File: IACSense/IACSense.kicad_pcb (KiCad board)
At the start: 2 copper layers, 57 parts, among them P1 CONN_01X03, P2 CONN_01X03, P3 zcd, P4 event, U1 MCP39F521, U2 MCP970x, U3 MCP1754, U4 PIC16F18323_QFN, Y1 4MHz

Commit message: Update IACSense
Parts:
- added D1: MB8S, Yame_library:MBxS, F.Cu at (212.5, 85.0)
- added P5: Prog, Yame_library:HE10_14-5C-2.54-MR, F.Cu at (167.0, 47.0)
- added P6: nRF24L01+, Yame_library:HE10_14-2x4C-2.54-MR, F.Cu at (167.0, 108.0)
- added P7: I2C, Yame_library:HE10_14-3C-2.54-MR, F.Cu at (168.0, 100.0)
- FB1, FB2, R1, R2: moved to B.Cu
- U3: footprint TO_SOT_Packages_THT:TO-220_Neutral123_Vertical -> Yame_library:SOT23-MR
- moved Y1 92.3 mm to (207.5, 34.0)
- moved C3 83.7 mm to (231.0, 91.0)
- moved R8 83.2 mm to (230.5, 91.0)
- moved D2 82.2 mm to (210.0, 50.5)
- moved FB4 81.8 mm to (200.0, 41.5)
- moved R16 76.4 mm to (201.0, 49.5)
- moved R6 76.0 mm to (187.0, 39.5)
- moved R4 74.9 mm to (192.0, 44.0)
- moved R3 74.8 mm to (197.0, 48.0)
- moved R15 70.0 mm to (190.5, 49.0)
- moved C2 69.6 mm to (185.5, 46.0)
- moved R5 68.7 mm to (181.0, 44.5)
- moved R19 67.8 mm to (176.0, 43.0)
- moved F1 67.7 mm to (215.0, 92.5)
- moved P2 67.5 mm to (200.5, 62.0), turned to 180 degrees
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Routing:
- net /Line: track 0.00 -> 87.8 mm
- net /Ground: track 0.00 -> 74.7 mm
- net Net-(FB4-Pad1): track 0.00 -> 56.7 mm
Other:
- board outline added: 29 x 83 mm
- rule via_min_size: 0.4 -> 0.5

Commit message: update IACSense
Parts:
- C1, C11, C13, C2, C4, D1, FB3, FB4, R3, R4, R5, R6, R7, R8, R9, U1, U3: moved to B.Cu
- P1: value CONN_01X03 -> IN
- P2: value CONN_01X03 -> OUT
- P6: footprint Yame_library:HE10_14-2x4C-2.54-MR -> Yame_library:NRF24L01+
- moved C4 61.9 mm to (197.8, 83.5)
- moved R7 59.1 mm to (197.2, 86.2), turned to 270 degrees
- moved P6 58.2 mm to (221.4, 87.5), turned to 180 degrees
- moved R9 57.2 mm to (197.8, 82.0)
- moved U1 54.4 mm to (204.8, 74.1), turned to 180 degrees
- moved C13 54.3 mm to (197.6, 97.4)
- moved C11 50.6 mm to (197.7, 99.3)
- moved D2 49.4 mm to (201.6, 99.2)
- moved FB1 45.9 mm to (213.8, 116.0), turned to 90 degrees
- moved R4 45.6 mm to (197.2, 89.3), turned to 270 degrees
- moved U3 45.3 mm to (197.4, 94.3), turned to 270 degrees
- moved FB2 43.8 mm to (206.2, 118.6), turned to 270 degrees
- moved C3 40.6 mm to (198.6, 115.3)
- moved C1 40.2 mm to (200.2, 76.5), turned to 270 degrees
- moved R2 38.5 mm to (203.3, 118.3)
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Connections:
- FB2 pad 2: Net-(FB2-Pad2) -> /Neutral
- VR1 pad 2: Net-(FB2-Pad2) -> /Neutral
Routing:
- net /Neutral: track 0.00 -> 58.2 mm
- net Net-(FB4-Pad1): track 56.7 -> 32.7 mm

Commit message: Update IACSense
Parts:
- added C21: 10u, Yame_library:SM0805-MR, F.Cu at (208.9, 85.7)
- added FB5: BLM18AG102SN1D, Yame_library:SM0603-MR, F.Cu at (187.2, 81.8)
- C11, C13, C4, R4, R7, R9, U1, U3: moved to F.Cu
- R2: footprint Yame_library:SM0603-MR -> Yame_library:SM1206-MR
- R20: moved to B.Cu
- moved C17 89.8 mm to (225.3, 78.4), turned to 180 degrees
- moved D3 86.9 mm to (229.4, 75.3), turned to 90 degrees
- moved C6 83.8 mm to (219.7, 74.3), turned to 270 degrees
- moved C7 74.9 mm to (219.7, 79.9), turned to 90 degrees
- moved P5 71.3 mm to (224.7, 89.0), turned to 270 degrees
- moved C12 68.3 mm to (204.7, 72.0), turned to 270 degrees
- moved R17 67.9 mm to (229.4, 78.4), turned to 270 degrees
- moved R11 66.1 mm to (211.3, 73.9), turned to 270 degrees
- moved R13 65.3 mm to (221.2, 70.2), turned to 270 degrees
- moved C8 64.4 mm to (203.8, 84.2), turned to 270 degrees
- moved C15 64.1 mm to (213.6, 89.8), turned to 270 degrees
- moved C16 63.7 mm to (206.1, 84.8), turned to 270 degrees
- moved C5 63.4 mm to (201.0, 82.3), turned to 270 degrees
- moved P7 63.2 mm to (220.4, 64.7)
- moved C20 62.8 mm to (208.7, 73.0)
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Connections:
- P1 pad 1: /Ground -> /Neutral
- P1 pad 3: /Neutral -> /Ground
- P2 pad 1: Net-(FB4-Pad1) -> /Ground
- P2 pad 3: /Ground -> Net-(FB4-Pad1)
- R19 pad 2: /Vtemp -> Net-(R18-Pad2)
- R4 pad 2: Net-(F1-Pad1) -> Net-(FB5-Pad1)
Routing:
- net /Line: track 87.8 -> 155.3 mm, vias 0 -> 1
- net /Ground: track 74.7 -> 141.2 mm
- net Net-(C10-Pad1): track 0.00 -> 49.4 mm
- net /3.3D: track 0.00 -> 43.8 mm, vias 0 -> 3
- net Net-(C3-Pad1): track 0.00 -> 29.9 mm
- net /SDA: track 0.00 -> 29.1 mm, vias 0 -> 2
- net /Neutral: track 58.2 -> 85.6 mm
- net GND: track 0.00 -> 27.4 mm, vias 0 -> 3
- net /SCL: track 0.00 -> 26.8 mm, vias 0 -> 2
- net Net-(R18-Pad2): track 0.00 -> 26.5 mm
- net Net-(FB4-Pad1): track 32.7 -> 14.6 mm
- net Net-(D1-Pad2): track 0.00 -> 17.6 mm
- net Net-(C6-Pad1): track 0.00 -> 15.7 mm
- net Net-(C7-Pad1): track 0.00 -> 15.1 mm
- net Net-(C4-Pad1): track 0.00 -> 12.5 mm
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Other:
- board size 29 x 83 mm -> 56.6 x 87.4 mm
- net class Default: via_dia 0.6 -> 0.7
- rule via_min_drill: 0.3 -> 0.4
- rule via_min_size: 0.5 -> 0.7

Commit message: Update IACSense
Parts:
- P7: footprint Yame_library:HE10_14-3C-2.54-MR -> Yame_library:HE10_14-4C-2.54-MR
- moved R15 15.7 mm to (229.9, 70.9)
- moved R16 10.7 mm to (229.9, 72.7)
- moved P7 7.09 mm to (226.8, 61.6)
- moved C17 1.41 mm to (226.7, 78.2), turned to 0 degrees
- moved P6 0.55 mm to (230.4, 110.8)
- moved C18 0.40 mm to (224.8, 80.1)
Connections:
- P7 pad 1: /SCL -> /3.3D
- P7 pad 2: /SDA -> /SCL
- P7 pad 3: GND -> /SDA
- U1 pad 29: (no net) -> GND
- U4 pad 17: (no net) -> GND
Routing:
- net /3.3D: track 43.8 -> 212.8 mm, vias 3 -> 5
- net /SCK: track 0.00 -> 58.1 mm, vias 0 -> 2
- net /MOSI: track 0.00 -> 56.7 mm
- net //CS: track 0.00 -> 53.7 mm, vias 0 -> 2
- net /MISO: track 0.00 -> 52.8 mm
- net /IRQ: track 0.00 -> 45.6 mm, vias 0 -> 4
- net /CE: track 0.00 -> 39.1 mm, vias 0 -> 4
- net GND: track 27.4 -> 66.1 mm, vias 3 -> 28
- net Net-(P5-Pad4): track 0.00 -> 37.9 mm
- net Net-(P5-Pad2): track 0.00 -> 18.3 mm, vias 0 -> 2
- net /SCL: track 26.8 -> 41.1 mm
- net Net-(P5-Pad1): track 0.00 -> 13.3 mm, vias 0 -> 2
- net /SDA: track 29.1 -> 39.2 mm
- net /3.3A: track 5.61 -> 12.2 mm, vias 0 -> 1
- net Net-(R15-Pad1): track 0.00 -> 4.55 mm
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
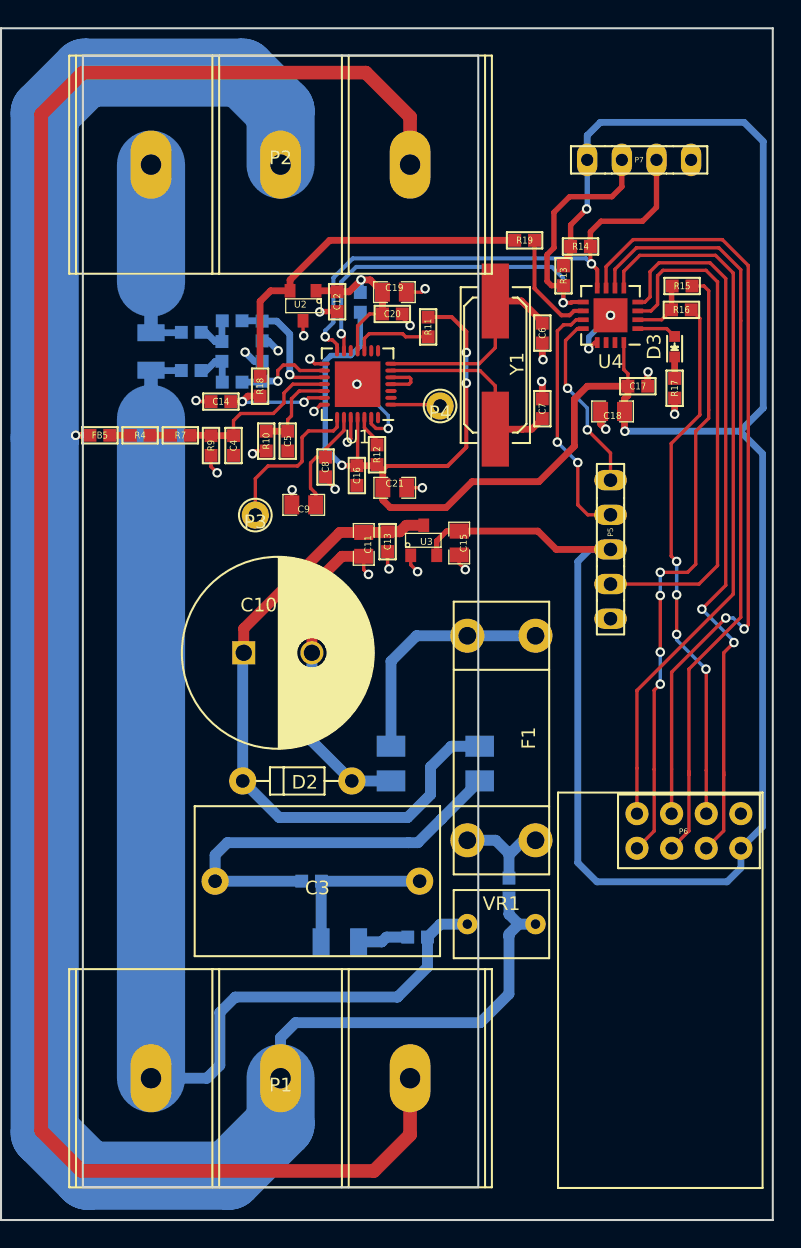
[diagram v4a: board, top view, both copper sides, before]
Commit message: Update IACSENSE and send to fab BancGeo & IACSense
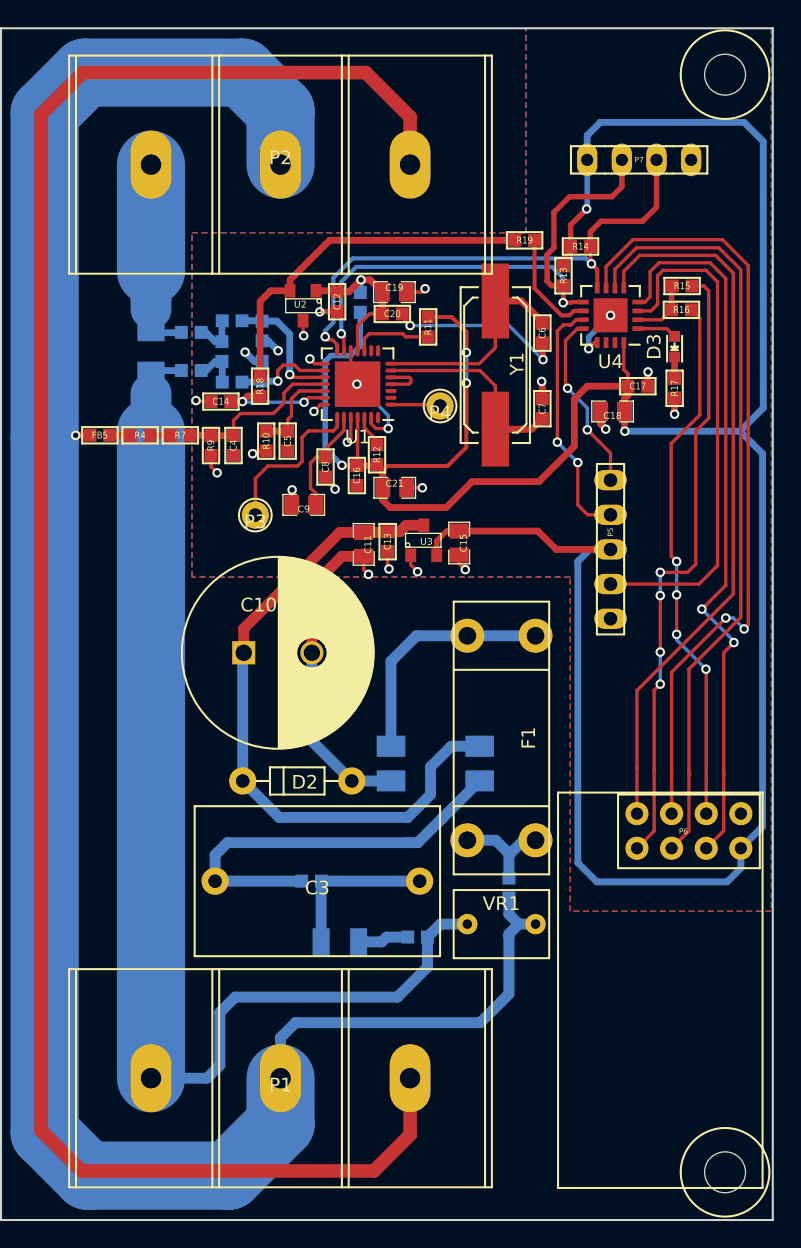
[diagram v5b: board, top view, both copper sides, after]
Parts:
- added MountingHole_3.5-6.5: VAL**, Yame_library:MountingHole_3-6.5, F.Cu at (233.1, 55.4)
- added MountingHole_3.5-6.5: VAL**, Yame_library:MountingHole_3-6.5, F.Cu at (233.1, 135.9)
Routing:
- net GND: track 66.1 -> 78.6 mm
- added copper zone on B.Cu, net GND
- added copper zone on F.Cu, net GND
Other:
- outline, holes or cut-outs redrawn
- net class Default: clearance 0.2 -> 0.195
- rule pad_to_mask_clearance: 0.2 -> 0.1
- rule trace_clearance: 0.2 -> 0.195

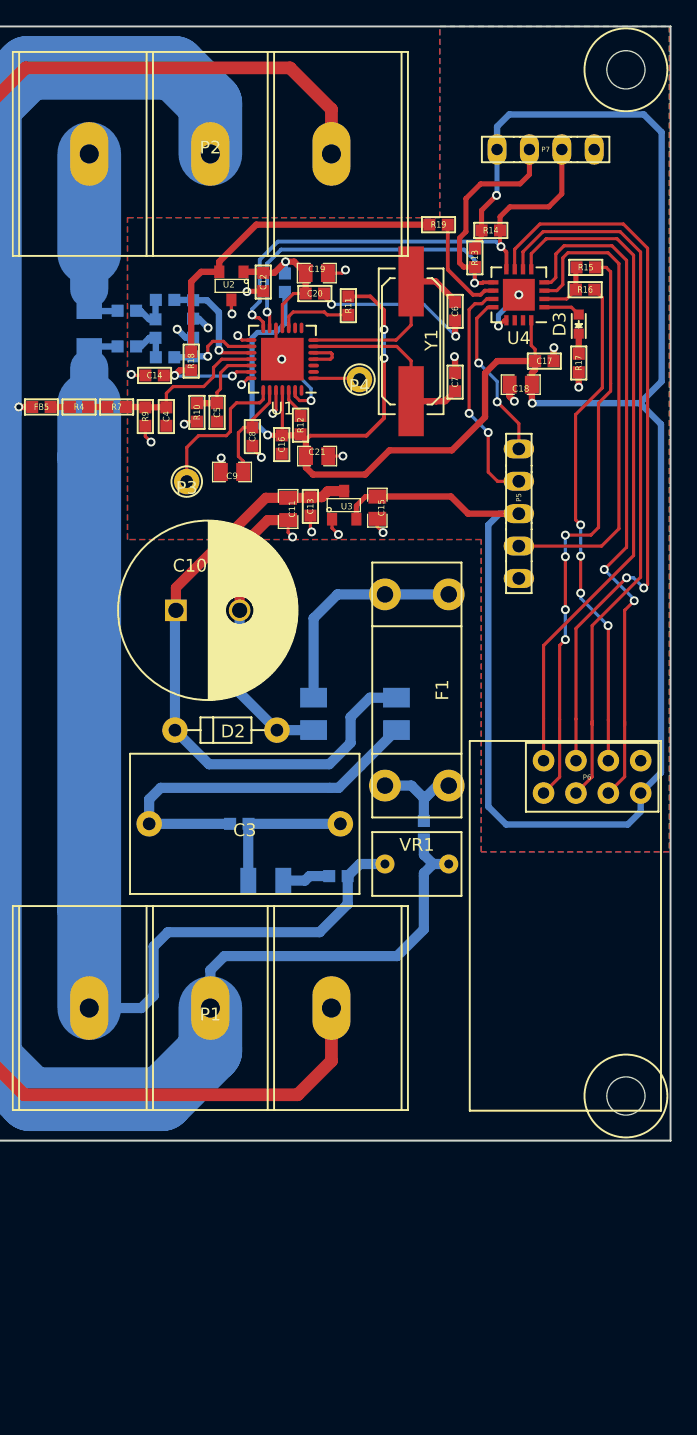
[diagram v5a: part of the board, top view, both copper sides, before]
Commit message: Update IACSense footprint
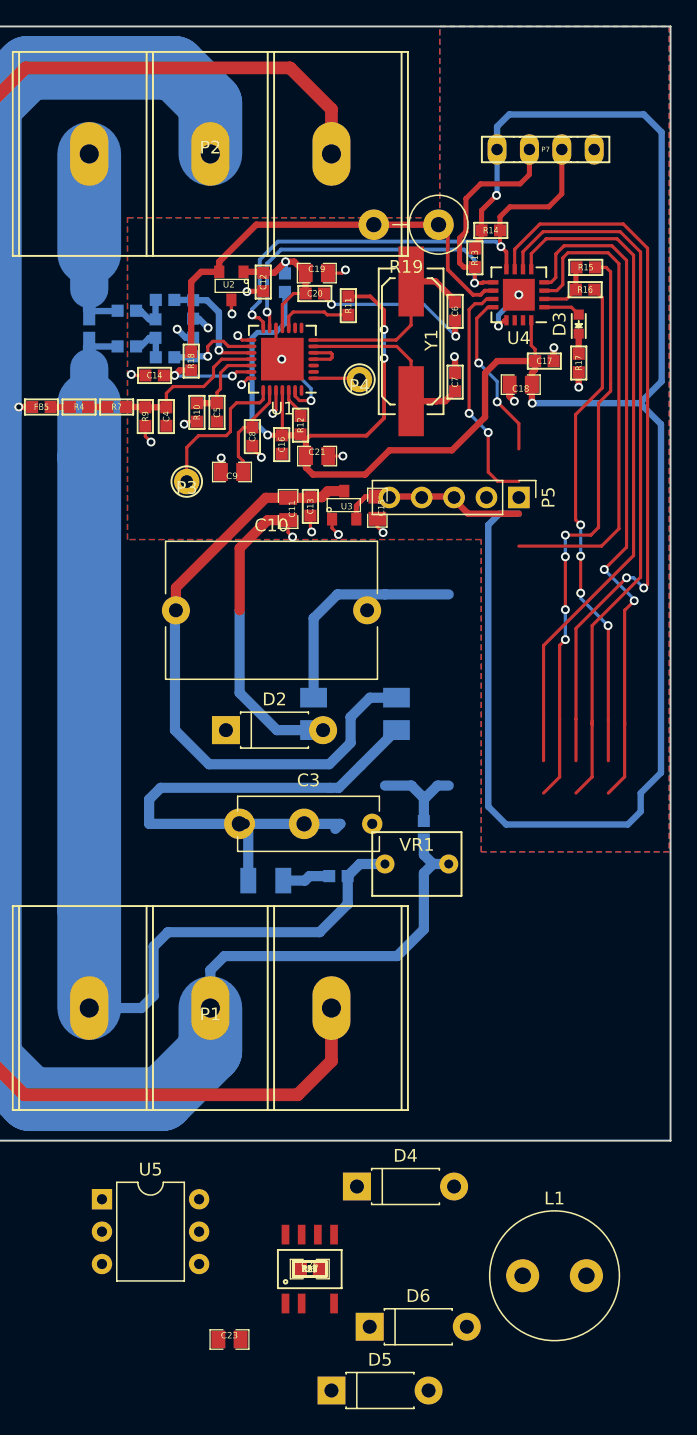
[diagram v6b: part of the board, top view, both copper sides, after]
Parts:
- removed F1: 0751.0062, Yame_library:Fuse_5x20
- removed MountingHole_3.5-6.5 (x2): VAL**, Yame_library:MountingHole_3-6.5
- removed P6: nRF24L01+, Yame_library:NRF24L01+
- added C22: 100n, Yame_library:SM0603-MR, F.Cu at (208.3, 149.5)
- added C23: 10u, Yame_library:SM0805-MR, F.Cu at (202.0, 155.0)
- added C26: 1u, Yame_library:SM0805-MR, F.Cu at (208.3, 149.5)
- added D4: 1N4007, Diodes_THT:D_DO-41_SOD81_P7.62mm_Horizontal, F.Cu at (212.0, 143.0)
- added D5: UF4005, Diodes_THT:D_DO-41_SOD81_P7.62mm_Horizontal, F.Cu at (210.0, 159.0)
- added D6: 1N4007, Diodes_THT:D_DO-41_SOD81_P7.62mm_Horizontal, F.Cu at (213.0, 154.0)
- added FB6: BLM18AG102SN1D, Yame_library:SM0603-MR, F.Cu at (208.3, 149.5)
- added L1: RLB0914-681KL, Inductors_THT:L_Radial_D10.0mm_P5.00mm_Fastron_07M, F.Cu at (225.0, 150.0)
- added R22: 100k, Yame_library:SM0603-MR, F.Cu at (208.3, 149.5)
- added R23: 2.49k, Yame_library:SM0603-MR, F.Cu at (208.3, 149.5)
- added R24: 3.48k, Yame_library:SM0603-MR, F.Cu at (208.3, 149.5)
- added R25: 1.6k, Yame_library:SM0603-MR, F.Cu at (208.3, 149.5)
- added U5: MOC3021M, Housings_DIP:DIP-6_W7.62mm, F.Cu at (192.0, 144.0)
- added U6: LNK320x, Yame_library:SO-8C-7, F.Cu at (208.3, 149.5)
- C10: value CP -> 100n; footprint Capacitors_ThroughHole:C_Radial_D14_L25_P5 -> Capacitors_THT:C_Rect_L16.5mm_W10.7mm_P15.00mm_MKT
- C11: value 10u -> 1u_400V
- C13: value 100n -> 1u_400V
- C3: value 0.68uF_X2_B32922C3684M -> 100n; footprint Yame_library:X2_15mm -> Capacitors_THT:C_Rect_L11.0mm_W4.2mm_P10.00mm_MKT
- D1: value MB8S -> Q_TRIAC_AAG
- D2: value BZX85C4V7 -> 1N4007; footprint Yame_library:DO-204AL -> Diodes_THT:D_DO-41_SOD81_P7.62mm_Horizontal
- P5: footprint Yame_library:HE10_14-5C-2.54-MR -> Pin_Headers:Pin_Header_Straight_1x05_Pitch2.54mm
- R1: value LRMAM1206-R002FT5 -> 680; footprint Yame_library:SM1206-MR -> Yame_library:SM0603-MR
- R18: value 100 -> 10k
- R19: value R -> 2.4k; footprint Yame_library:SM0603-MR -> Resistors_THT:R_Axial_DIN0414_L11.9mm_D4.5mm_P5.08mm_Vertical
- R2: value 100_0.5W_1206 -> FC4L32R002GER
- R20: value 33 -> EMC2-8R2K
- R8: value R -> 680; footprint Yame_library:SM0603-MR -> Resistors_THT:R_Axial_DIN0414_L11.9mm_D4.5mm_P5.08mm_Vertical
- U3: value MCP1754 -> MCP1754ST-3302E/CB
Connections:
- C10 pad 1: Net-(C10-Pad1) -> /Line
- C10 pad 2: GND -> Net-(C10-Pad2)
- C11 pad 1: Net-(C10-Pad1) -> Net-(C11-Pad1)
- C11 pad 2: GND -> Net-(C11-Pad2)
- C13 pad 1: Net-(C10-Pad1) -> Net-(C13-Pad1)
- C13 pad 2: GND -> Net-(C11-Pad2)
- C3 pad 1: Net-(C3-Pad1) -> /Line
- C3 pad 2: Net-(C3-Pad2) -> Net-(C10-Pad2)
- D1 pad 1: GND -> Net-(D1-Pad1)
- D1 pad 2: Net-(D1-Pad2) -> /Line
- D1 pad 3: Net-(C10-Pad1) -> Net-(D1-Pad3)
- D1 pad 4: Net-(C3-Pad1) -> (no net)
- D2 pad 1: Net-(C10-Pad1) -> Net-(C11-Pad1)
- D2 pad 2: GND -> Net-(D2-Pad2)
- FB1 pad 2: Net-(F1-Pad1) -> Net-(FB1-Pad2)
- FB2 pad 1: Net-(FB2-Pad1) -> Net-(D4-Pad1)
- FB3 pad 1: /Neutral -> Net-(FB3-Pad1)
- P1 pad 1: /Neutral -> Net-(P1-Pad1)
- P2 pad 1: /Ground -> /Neutral
- P2 pad 2: /Line -> Net-(D1-Pad1)
- P2 pad 3: Net-(FB4-Pad1) -> /Ground
- R1 pad 1: /Neutral -> /Out_SW
- R1 pad 2: Net-(FB4-Pad1) -> Net-(R1-Pad2)
- R19 pad 1: Net-(R19-Pad1) -> Net-(D1-Pad1)
- R19 pad 2: Net-(R18-Pad2) -> Net-(C10-Pad2)
- R2 pad 1: Net-(C3-Pad2) -> Net-(P1-Pad1)
- R2 pad 2: Net-(FB2-Pad1) -> Net-(FB3-Pad1)
- R20 pad 1: /3.3A -> Net-(D2-Pad2)
- R20 pad 2: /3.3D -> Net-(FB1-Pad2)
- R8 pad 1: Net-(C3-Pad1) -> Net-(R8-Pad1)
- R8 pad 2: Net-(C3-Pad2) -> Net-(C10-Pad2)
- U3 pad 3: Net-(C10-Pad1) -> /+5V
- U4 pad 1: Net-(D3-Pad2) -> Net-(R15-Pad1)
- U4 pad 10: Net-(R19-Pad1) -> /SCL
- U4 pad 2: Net-(R15-Pad1) -> /SDA
- U4 pad 4: //CS -> /Rx_BL
- U4 pad 5: /MISO -> /Tx_BL
- U4 pad 6: /MOSI -> /Out_SW
- U4 pad 7: /SCK -> Net-(U4-Pad7)
- U4 pad 8: /SDA -> Net-(U4-Pad8)
- U4 pad 9: /SCL -> /Vtemp
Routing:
- net /Ground: track 141.2 -> 12.0 mm
- net /Neutral: track 85.6 -> 164.4 mm
- net Net-(U4-Pad7): track 0.00 -> 58.1 mm, vias 0 -> 2
- net /SCK: track 58.1 -> 0.00 mm, vias 2 -> 0
- net /Out_SW: track 0.00 -> 56.7 mm
- net /MOSI: track 56.7 -> 0.00 mm
- net /Line: track 155.3 -> 209.9 mm
- net /Rx_BL: track 0.00 -> 53.7 mm, vias 0 -> 2
- net //CS: track 53.7 -> 0.00 mm, vias 2 -> 0
- net /Tx_BL: track 0.00 -> 52.8 mm
- net /MISO: track 52.8 -> 0.00 mm
- net Net-(C10-Pad1): track 49.4 -> 0.00 mm
- net Net-(FB3-Pad1): track 0.00 -> 48.1 mm
- net Net-(R8-Pad1): track 0.00 -> 42.2 mm
- net Net-(D1-Pad1): track 0.00 -> 34.5 mm
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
